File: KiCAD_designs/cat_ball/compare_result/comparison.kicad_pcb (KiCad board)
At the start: 2 copper layers, 35 x 34.7 mm, 35 parts, among them J1 B2B-PH-SM4-TBLFSN, J2 B2B-PH-SM4-TBLFSN, U1 ATMEGA328P-AU, U2 MX1508

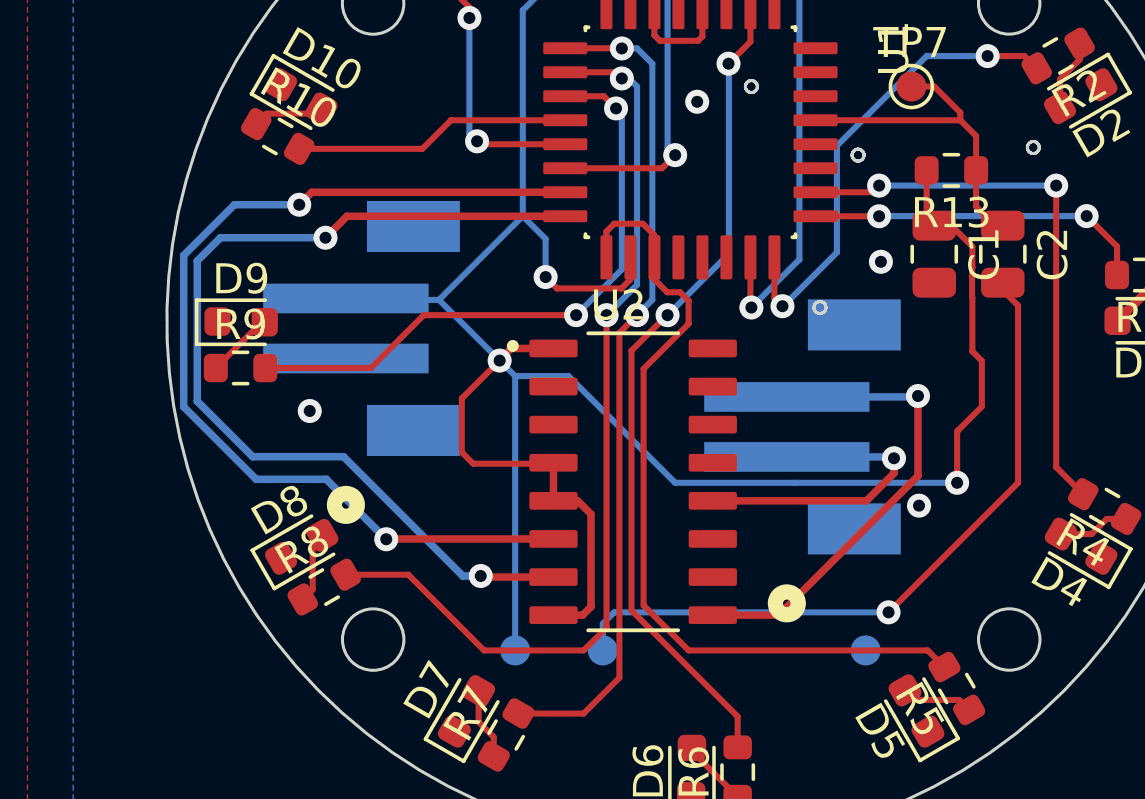
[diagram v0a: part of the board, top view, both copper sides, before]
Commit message: changed cat ball via size
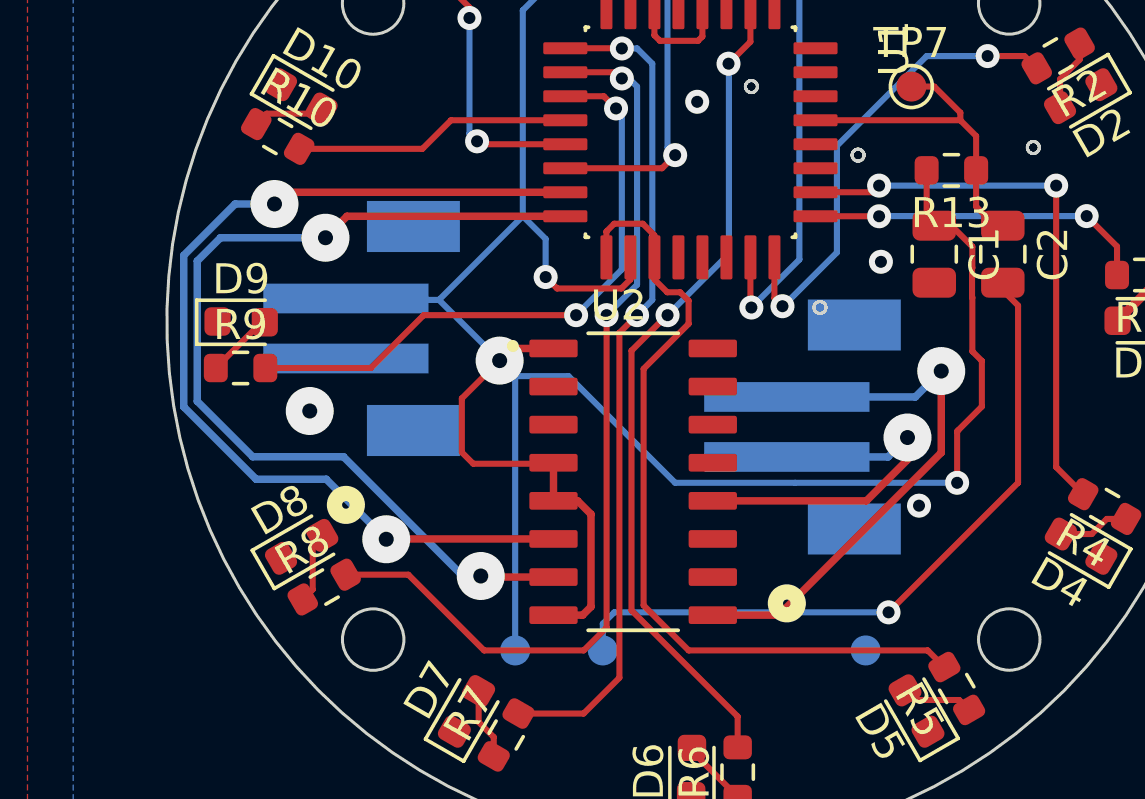
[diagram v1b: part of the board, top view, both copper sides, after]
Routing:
- net Net-(U2A-OUTB2): track 15.8 -> 18.1 mm
- net Net-(U2A-OUTA2): track 10.5 -> 12.1 mm

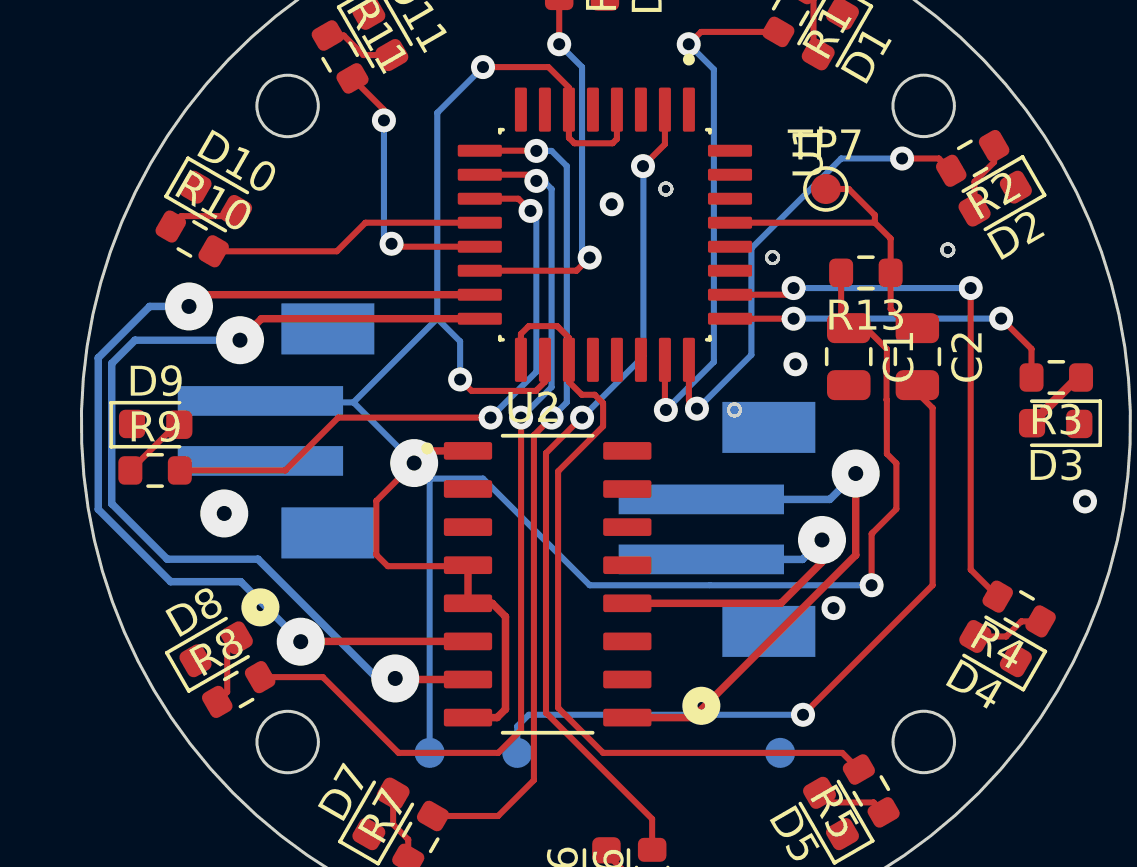
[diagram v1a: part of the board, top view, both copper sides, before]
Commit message: Exported edge cuts gerber now includes vias present on the new board and not on the old board as well
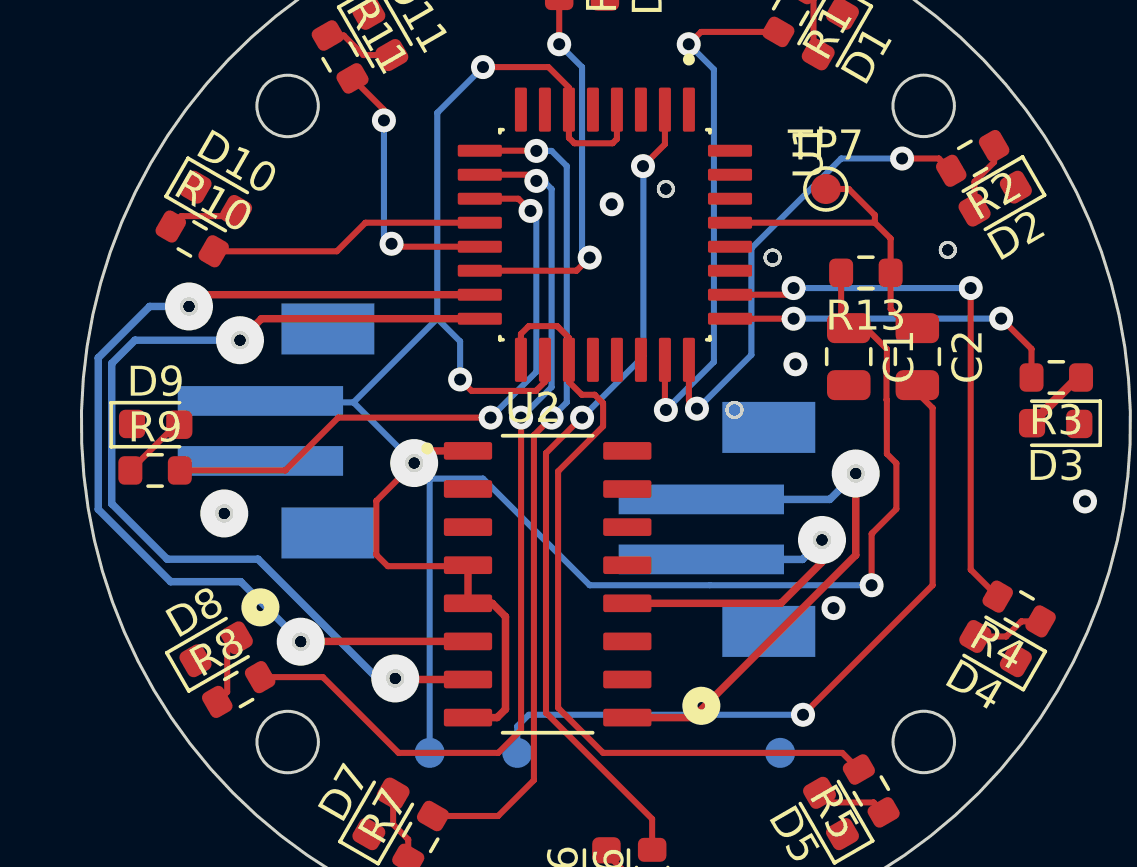
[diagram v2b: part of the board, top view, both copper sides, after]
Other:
- outline, holes or cut-outs redrawn

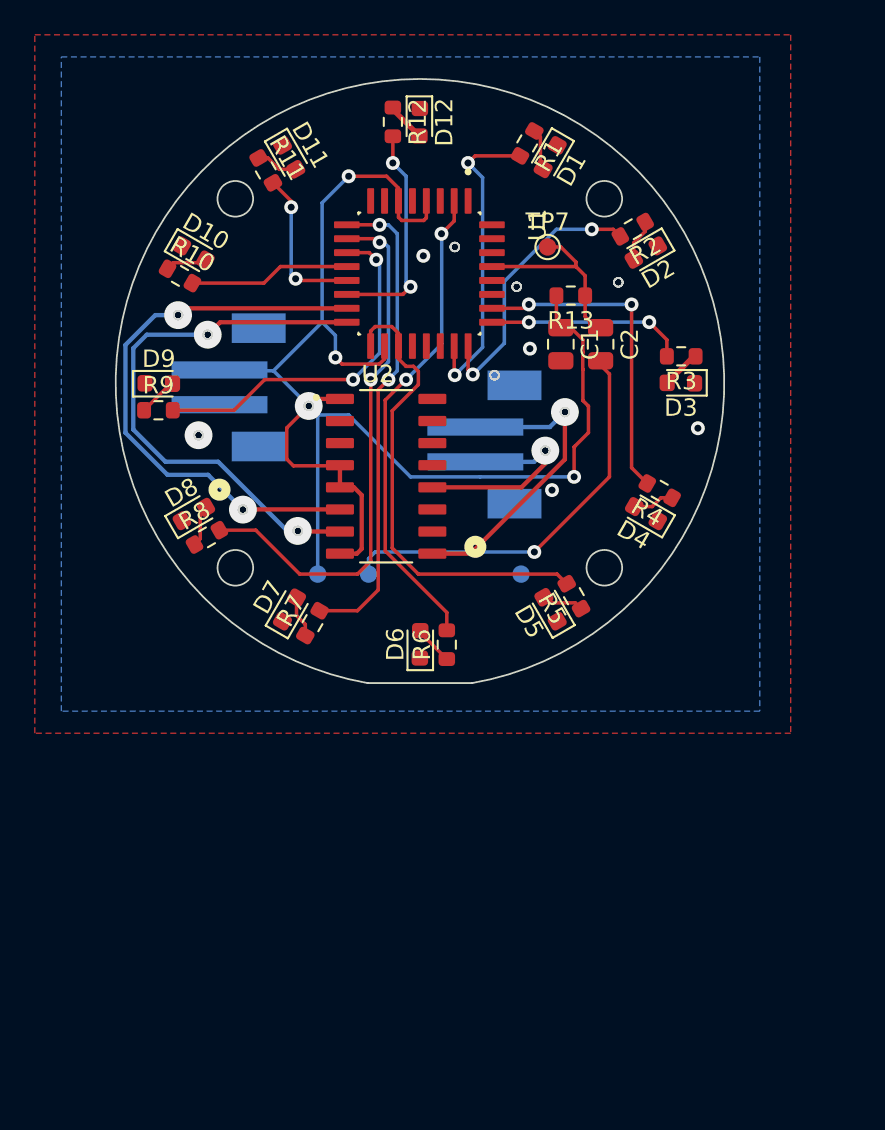
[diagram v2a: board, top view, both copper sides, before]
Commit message: catball thicker traces
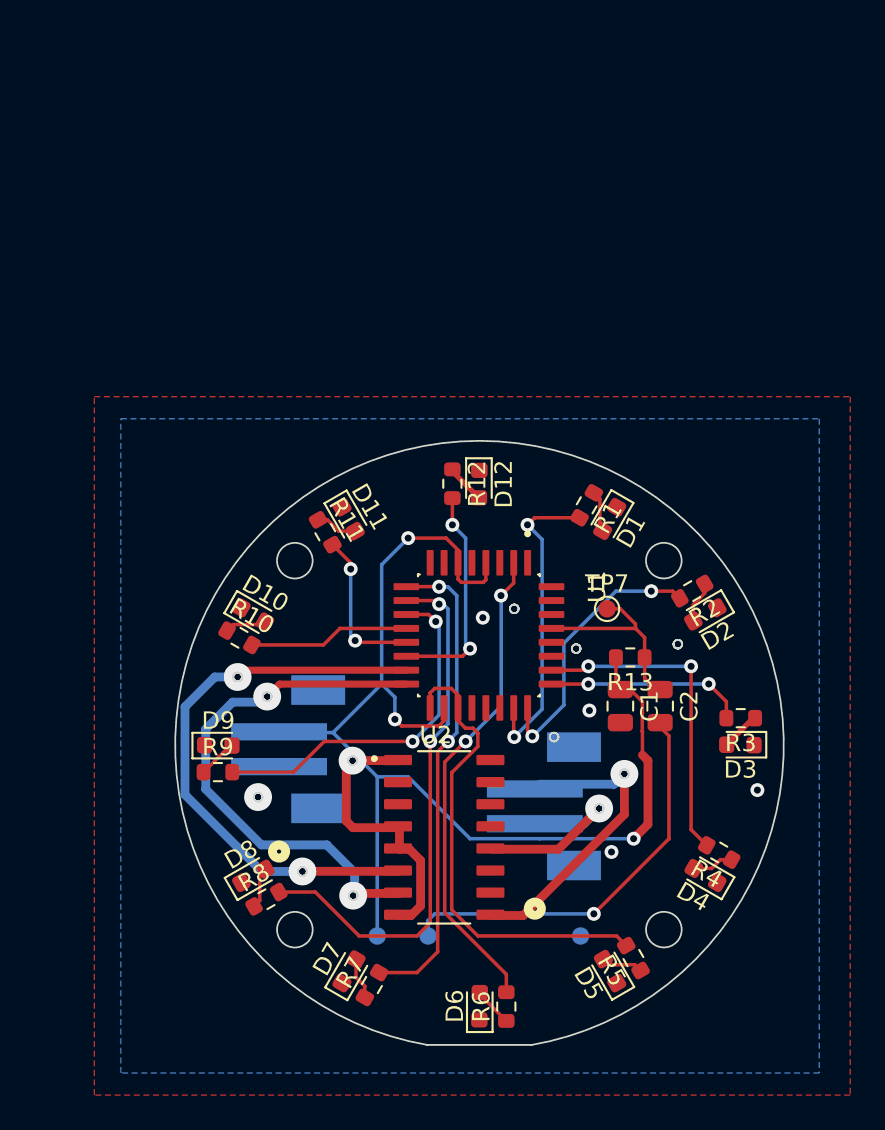
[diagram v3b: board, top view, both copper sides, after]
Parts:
- J1, J2: footprint esp_lib:B2B-PH-SM4-TBLFSN_JST -> IO_watch_cat_ball:B2B-PH-SM4-TBLFSN_JST
- U2: footprint esp_lib:MX1508 -> IO_watch_cat_ball:MX1508
- moved C1 21.1 mm to (152.4, 94.2)
- moved C2 21.1 mm to (154.7, 94.2)
- moved D3 21.1 mm to (159.3, 96.5)
- moved D5 21.1 mm to (151.8, 109.5)
- moved D7 21.1 mm to (136.8, 109.5)
- moved D9 21.1 mm to (129.3, 96.5)
- moved R13 21.1 mm to (153.0, 91.4)
- moved R2 21.1 mm to (156.5, 87.6)
- moved R6 21.1 mm to (145.9, 111.5)
- moved R7 21.1 mm to (138.1, 110.3)
- moved TP7 21.1 mm to (151.6, 88.7)
- moved D1 21.1 mm to (151.8, 83.5)
- moved D11 21.1 mm to (136.8, 83.5)
- moved D2 21.1 mm to (157.3, 89.0)
- moved D4 21.1 mm to (157.3, 104.0)
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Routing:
- net Net-(U2A-OUTA2): track 12.1 -> 11.2 mm
- net /D12: track 31.9 -> 31.1 mm
- net VCC: track 89.2 -> 89.9 mm
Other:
- outline, holes or cut-outs redrawn
